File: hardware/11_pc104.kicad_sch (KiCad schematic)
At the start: 1 part, among them J10 PC104-Mainboard

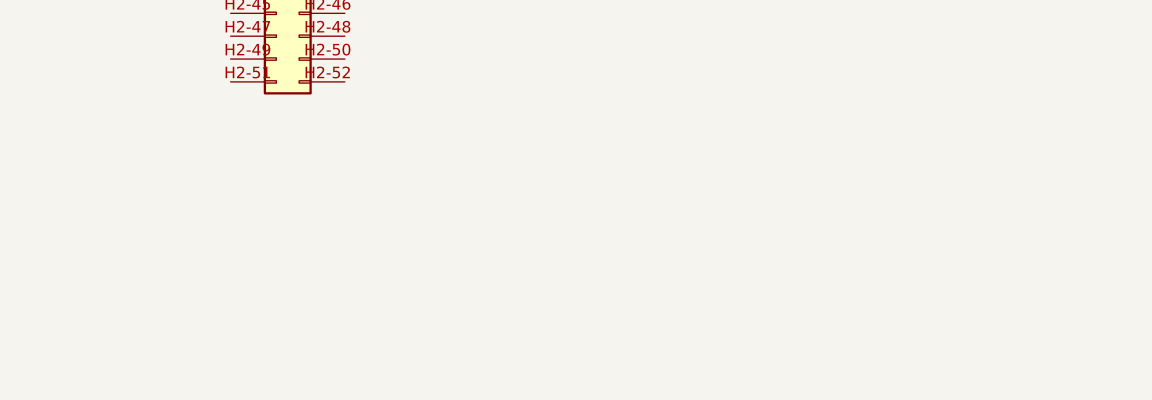
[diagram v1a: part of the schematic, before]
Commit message: Updated sheet names, added s-band initial block diagram
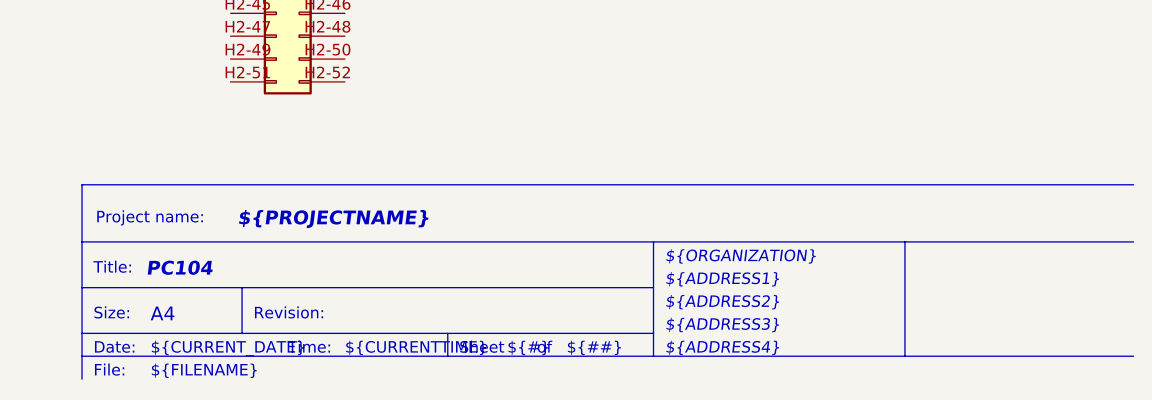
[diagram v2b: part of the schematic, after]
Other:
- note added: "${##}"
- note added: "${#}"
- note added: "${ADDRESS1}"
- note added: "${ADDRESS2}"
- note added: "${ADDRESS3}"
- note added: "${ADDRESS4}"
- note added: "${CURRENTTIME}"
- note added: "${CURRENT_DATE}"
- note added: "${FILENAME}"
- note added: "${ORGANIZATION}"
- note added: "${PROJECTNAME}"
- note added: "${REVISION}"
- note added: "${TITLE}"
- note added: "A4"
- note added: "Date:"
- note added: "File:"
- note added: "Project name:"
- note added: "Revision:"
- note added: "Sheet"
- note added: "Size:"
- note added: "Time:"
- note added: "Title:"
- note added: "of"
- title: (none) -> PC104
